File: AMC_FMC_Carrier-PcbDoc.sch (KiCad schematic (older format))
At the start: 15 parts

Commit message: Rename library AMC_FMC_Carrier-PcbDoc-rescue as marble_misc
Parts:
- S1: symbol AMC_FMC_Carrier-PcbDoc-rescue:HDT0001-HDT0001 -> marble_misc:HDT0001-HDT0001
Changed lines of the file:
@@
 FMC2_PRSNT_M2C_L
 $Comp
-L AMC_FMC_Carrier-PcbDoc-rescue:HDT0001-HDT0001 S1
+L marble_misc:HDT0001-HDT0001 S1
 U 1 1 5DAB8DC7
 P 2950 9200

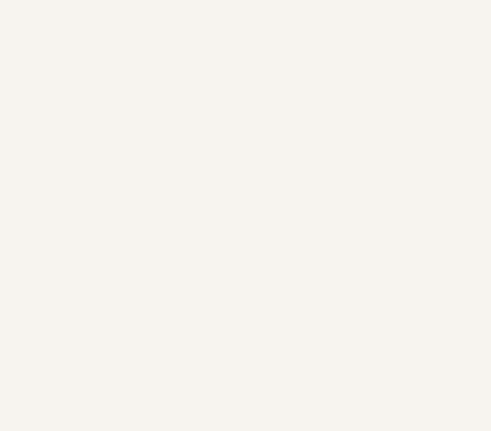
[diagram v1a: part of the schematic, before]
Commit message: schematic: add `branch: fab2` label
tiny change to schematic results in a huge diff :p
This will be my working version now.
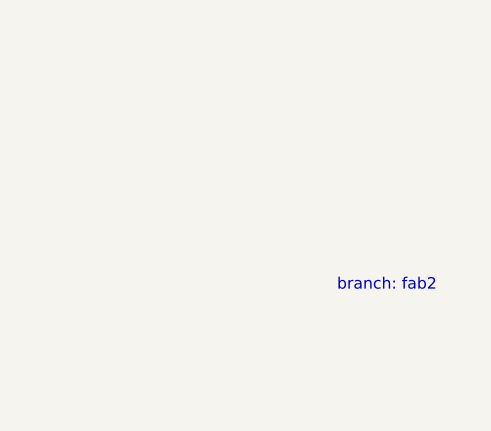
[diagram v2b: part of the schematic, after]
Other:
- note added: "branch: fab2"
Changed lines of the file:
@@
 EESchema Schematic File Version 4
-LIBS:AMC_FMC_Carrier-PcbDoc-cache
 EELAYER 30 0
 EELAYER END
@@
 Wire Notes Line
 	12450 8450 12950 8450
+Text Notes 18700 15200 0    50   ~ 0
+branch: fab2
 $EndSCHEMATC

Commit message: SCH: add mounting hole B1 - B10
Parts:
- added B10: PLATED_HOLE2.8_PAD0, Marble:HOLE2.8_PAD0, symbol Pads:PLATED_HOLE2.8_PAD0
- added B9: SLOT_2_11, Marble:HOLE2_SLOT11, symbol Pads:SLOT_2_11
- B1, B2, B3, B4, B5, B6, B7, B8: footprint Pads:MTG270_500 -> Marble:HOLE2.7_PAD5.0; Case ~~ -> (none); Comment ~~ -> (none); ComponentLink1Description ~~ -> (none); ComponentLink2Description ~~ -> (none); Database Table Name (none) -> Pads; Footprint Library (none) -> Pads; Library Name Pads -> Eletro-mechanical.DbLib; Manufacturer ~~ -> (none); Manufacturer Part Number ~~ -> (none); Manufacturer1 ComponentHeight ~~ -> (none); Manufacturer1 Example ~~ -> (none); Manufacturer1 Part Number ~~ -> (none); SCEM ~~ -> (none); Sense Comment ~~ -> (none); Status Comment ~~ -> (none)
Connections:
- wire segments 364 -> 366

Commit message: Configure S1 as dnf for standalone builds
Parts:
- S1: config (none) -> -standalone
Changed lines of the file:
@@
 F 12 "611-HDT0001" H 4000 8300 50  0001 L CNN "Mouser Part Number"
 F 13 "https://www.mouser.com/Search/Refine.aspx?Keyword=611-HDT0001" H 4000 8200 50  0001 L CNN "Mouser Price/Stock"
+F 14 "-standalone" H 2950 9200 50  0001 C CNN "config"
 	1    2950 9200
 	-1   0    0    -1

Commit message: Convert all footprints to use Marble nickname
Includes both .sch and .lib files
Includes both bare footprint names and those with CERN-like nicknames
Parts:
- FTG1, FTG2: footprint Pads:FIDUCIAL_TOP_S200-400 -> Marble:FIDUCIAL_TOP_S200-400
- FTG3, FTG4: footprint Pads:FIDUCIAL_BOT_S200-400 -> Marble:FIDUCIAL_BOT_S200-400
- R243, R244: footprint RESC3216X65N -> Marble:RESC3216X65N
- S1: footprint HDT0001:HDT0001 -> Marble:HDT0001
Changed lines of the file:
@@
 F 0 "S1" H 3550 9465 50  0000 C CNN
 F 1 "HDT0001" H 3550 9374 50  0000 C CNN
-F 2 "HDT0001:HDT0001" H 4000 9300 50  0001 L CNN
+F 2 "Marble:HDT0001" H 4000 9300 50  0001 L CNN
 F 3 "https://www.ckswitches.com/media/1307/hdt.pdf" H 4000 9200 50  0001 L CNN
 F 4 "HDT0001 (Detector Switches)" H 4000 9100 50  0001 L CNN "Description"
@@
 F 0 "R243" H 2500 14747 50  0000 C CNN
 F 1 "R1206_1M_1%_0.25W_100PPM" H 2350 14340 60  0001 L CNN
-F 2 "RESC3216X65N" H 2350 13530 60  0001 L CNN
+F 2 "Marble:RESC3216X65N" H 2350 13530 60  0001 L CNN
 F 3 "\\\\cern.ch\\dfs\\Applications\\Altium\\Datasheets\\R1206_NIC_NRC.pdf" H 2350 14160 60  0001 L CNN
 F 4 "1M" H 2500 14656 50  0000 C CNN "~"
@@
 F 0 "R244" H 3300 14747 50  0000 C CNN
 F 1 "R1206_1M_1%_0.25W_100PPM" H 3150 14340 60  0001 L CNN
-F 2 "RESC3216X65N" H 3150 13530 60  0001 L CNN
+F 2 "Marble:RESC3216X65N" H 3150 13530 60  0001 L CNN
 F 3 "\\\\cern.ch\\dfs\\Applications\\Altium\\Datasheets\\R1206_NIC_NRC.pdf" H 3150 14160 60  0001 L CNN
 F 4 "1M" H 3300 14656 50  0000 C CNN "~"
@@
 F 0 "FTG1" H 2888 14900 50  0000 L CNN
 F 1 "FIDUCIAL_TARGET_C100-200" H 2800 14750 60  0001 L CNN
-F 2 "Pads:FIDUCIAL_TOP_S200-400" H 2800 13940 60  0001 L CNN
+F 2 "Marble:FIDUCIAL_TOP_S200-400" H 2800 13940 60  0001 L CNN
 F 3 "" H 2800 14570 60  0001 L CNN
 F 4 "~~" H 2800 14480 60  0001 L CNN "Pole4"
@@
 F 0 "FTG2" H 3238 14900 50  0000 L CNN
 F 1 "FIDUCIAL_TARGET_C100-200" H 3150 14750 60  0001 L CNN
-F 2 "Pads:FIDUCIAL_TOP_S200-400" H 3150 13940 60  0001 L CNN
+F 2 "Marble:FIDUCIAL_TOP_S200-400" H 3150 13940 60  0001 L CNN
 F 3 "" H 3150 14570 60  0001 L CNN
 F 4 "~~" H 3150 14480 60  0001 L CNN "Pole4"
@@
 F 0 "FTG3" H 3588 14900 50  0000 L CNN
 F 1 "FIDUCIAL_TARGET_C100-200" H 3500 14750 60  0001 L CNN
-F 2 "Pads:FIDUCIAL_BOT_S200-400" H 3500 13940 60  0001 L CNN
+F 2 "Marble:FIDUCIAL_BOT_S200-400" H 3500 13940 60  0001 L CNN
 F 3 "" H 3500 14570 60  0001 L CNN
 F 4 "~~" H 3500 14480 60  0001 L CNN "Pole4"
@@
 F 0 "FTG4" H 3938 14900 50  0000 L CNN
 F 1 "Pads:FIDUCIAL_BOT_S200-400" H 3850 14750 60  0001 L CNN
-F 2 "Pads:FIDUCIAL_BOT_S200-400" H 3850 13940 60  0001 L CNN
+F 2 "Marble:FIDUCIAL_BOT_S200-400" H 3850 13940 60  0001 L CNN
 F 3 "" H 3850 14570 60  0001 L CNN
 F 4 "~~" H 3850 14480 60  0001 L CNN "Pole4"

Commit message: add  field to mounting hole symbols
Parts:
- B1, B10, B2, B3, B4, B5, B6, B7, B8, B9: config (none) -> dnf
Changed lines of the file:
@@
 F 42 "Pads" H 2800 15500 50  0001 C CNN "Database Table Name"
 F 43 "Pads" H 2800 15500 50  0001 C CNN "Footprint Library"
+F 44 "dnf" H 2800 15500 50  0001 C CNN "config"
 	1    2800 15500
 	1    0    0    -1
@@
 F 42 "Pads" H 2950 15500 50  0001 C CNN "Database Table Name"
 F 43 "Pads" H 2950 15500 50  0001 C CNN "Footprint Library"
+F 44 "dnf" H 2950 15500 50  0001 C CNN "config"
 	1    2950 15500
 	1    0    0    -1
@@
 F 42 "Pads" H 3100 15500 50  0001 C CNN "Database Table Name"
 F 43 "Pads" H 3100 15500 50  0001 C CNN "Footprint Library"
+F 44 "dnf" H 3100 15500 50  0001 C CNN "config"
 	1    3100 15500
 	1    0    0    -1
@@
 F 42 "Pads" H 3250 15500 50  0001 C CNN "Database Table Name"
 F 43 "Pads" H 3250 15500 50  0001 C CNN "Footprint Library"
+F 44 "dnf" H 3250 15500 50  0001 C CNN "config"
 	1    3250 15500
 	1    0    0    -1
@@
 F 42 "Pads" H 2800 15250 50  0001 C CNN "Database Table Name"
 F 43 "Pads" H 2800 15250 50  0001 C CNN "Footprint Library"
+F 44 "dnf" H 2800 15250 50  0001 C CNN "config"
 	1    2800 15250
 	1    0    0    -1
@@
 F 42 "Pads" H 2950 15250 50  0001 C CNN "Database Table Name"
 F 43 "Pads" H 2950 15250 50  0001 C CNN "Footprint Library"
+F 44 "dnf" H 2950 15250 50  0001 C CNN "config"
 	1    2950 15250
 	1    0    0    -1
@@
 F 42 "Pads" H 3100 15250 50  0001 C CNN "Database Table Name"
 F 43 "Pads" H 3100 15250 50  0001 C CNN "Footprint Library"
+F 44 "dnf" H 3100 15250 50  0001 C CNN "config"
 	1    3100 15250
 	1    0    0    -1
@@
 F 42 "Pads" H 3250 15250 50  0001 C CNN "Database Table Name"
 F 43 "Pads" H 3250 15250 50  0001 C CNN "Footprint Library"
+F 44 "dnf" H 3250 15250 50  0001 C CNN "config"
 	1    3250 15250
 	1    0    0    -1
@@
 F 3 "" H 3400 15195 50  0001 L CNN
 F 4 "This work is licensed under the Creative Commons CC-BY-SA 4.0 License. To the extent that circuit schematics that use Licensed Material can be considered to be ‘Adapted Material’, then the copyright holder waives article 3.b of the license with respect to these schematics." H 3400 12495 50  0001 L CNN "License"
+F 5 "dnf" H 3400 15500 50  0001 C CNN "config"
 	1    3400 15500
 	1    0    0    -1
@@
 F 3 "" H 3400 14945 50  0001 L CNN
 F 4 "This work is licensed under the Creative Commons CC-BY-SA 4.0 License. To the extent that circuit schematics that use Licensed Material can be considered to be ‘Adapted Material’, then the copyright holder waives article 3.b of the license with respect to these schematics." H 3400 12245 50  0001 L CNN "License"
+F 5 "dnf" H 3400 15250 50  0001 C CNN "config"
 	1    3400 15250
 	1    0    0    -1

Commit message: Get rid of "~" attribute in instances
This makes instances line up better with our library
Use a very short python program to rename "~" to "Val" and remove the old "Val".
Required a little pre-patch to correctly handle R297 R298 R299 R300 R162 R274 R197 R198, which had no "~" field.
No net changes to "Val" field contents.
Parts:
- R243, R244: ~ 1M -> (none)
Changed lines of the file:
@@
 F 2 "Marble:RESC3216X65N" H 2350 13530 60  0001 L CNN
 F 3 "\\\\cern.ch\\dfs\\Applications\\Altium\\Datasheets\\R1206_NIC_NRC.pdf" H 2350 14160 60  0001 L CNN
-F 4 "1M" H 2500 14656 50  0000 C CNN "~"
+F 4 "1M" H 2500 14656 50  0000 C CNN "Val"
 F 5 "R1206_1M_1%_0.25W_100PPM" H 2350 14070 60  0001 L CNN "Part Number"
 F 6 "Resistor - 1%" H 2350 13980 60  0001 L CNN "Library Ref"
@@
 F 13 "PcbLib\\Resistors SMD.PcbLib" H 2350 13260 60  0001 L CNN "Footprint Path"
 F 14 "RESC3216X65N" H 2350 13170 60  0001 L CNN "Footprint Ref"
-F 15 "1M" H 2350 13080 60  0001 L CNN "Val"
 F 16 "Preferred" H 2350 12990 60  0001 L CNN "Status"
 F 17 "0.25W" H 2350 12900 60  0001 L CNN "Power"
@@
 F 2 "Marble:RESC3216X65N" H 3150 13530 60  0001 L CNN
 F 3 "\\\\cern.ch\\dfs\\Applications\\Altium\\Datasheets\\R1206_NIC_NRC.pdf" H 3150 14160 60  0001 L CNN
-F 4 "1M" H 3300 14656 50  0000 C CNN "~"
+F 4 "1M" H 3300 14656 50  0000 C CNN "Val"
 F 5 "R1206_1M_1%_0.25W_100PPM" H 3150 14070 60  0001 L CNN "Part Number"
 F 6 "Resistor - 1%" H 3150 13980 60  0001 L CNN "Library Ref"
@@
 F 13 "PcbLib\\Resistors SMD.PcbLib" H 3150 13260 60  0001 L CNN "Footprint Path"
 F 14 "RESC3216X65N" H 3150 13170 60  0001 L CNN "Footprint Ref"
-F 15 "1M" H 3150 13080 60  0001 L CNN "Val"
 F 16 "Preferred" H 3150 12990 60  0001 L CNN "Status"
 F 17 "0.25W" H 3150 12900 60  0001 L CNN "Power"
